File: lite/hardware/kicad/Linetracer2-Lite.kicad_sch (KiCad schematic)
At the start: 30 parts, among them J1 BATTERY (AA x3, XH 2P), J2 I2C (0.96in OLED order), M1 LEFT motor FA-130RA, M2 RIGHT motor FA-130RA, Q1 2SC1815-GR, SW1 START, U1 Raspberry Pi Pico, U2 AE-TC78H653FTG

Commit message: Lite rev.L2: XIAO ESP32C6 と LBR-127HLD に変更、子ども向けに配置・シルクを見直し
- マイコンを Seeed Studio XIAO ESP32C6（秋月 129481）に。ピンヘッダなしで基板にじかにはんだ付け
  （自作フットプリント: 裏のテストパッドの下は銅禁止、USB の足の逃げ穴、アンテナの下は両面銅なし）
- フォトリフレクタを LBR-127HLD（秋月 104500）に。背が 5.6 mm あるのでスキッドを 7.5 mm に
  （skid_clip_h70/h75/h80.stl、ロボットは後ろに 2.9° 傾く。傾きとすき間は scad で計算）
- いらない部品: I2C の穴 J2 を削除。電池電圧の測定はなし（XIAO の ADC 3 本をセンサーで使い切る）
- ピン割り当ては ESP32-C6 の起動時の状態に合わせ、どの瞬間もモーターが回らないようにした
- 基板を 65 x 100 mm の長方形に（面積 -27%、3D プリント部品はそのまま）、抵抗を 6 mm おきに
- シルクは記号だけ（つくる順番の数字、＋、LED の絵、抵抗の 3 本目の色）。説明は手順書 lite/docs/assembly.md
- gen_3d.py の 3D モデルの位置ずれを修正（KiCad は VRML の translation に scale をかけない）
- ERC 0、DRC 0（警告 0・未接続 0）。MicroPython (ESP32_GENERIC_C6) のライブラリとサンプルを移植

Co-Authored-By: Claude Opus 5.5 <noreply@anthropic.com>
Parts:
- removed J2: I2C (0.96in OLED order), Connector_PinHeader_2.54mm:PinHeader_1x04_P2.54mm_Vertical, symbol Connector_Generic:Conn_01x04
- C2: Note hold-up for Pico when motors pull the battery down -> hold-up for the XIAO when motors pull the battery down
- PS1, PS2, PS3: value LBR-123F -> LBR-127HLD; footprint Linetracer2:LBR-123F -> Linetracer2:LBR-127HLD; symbol Linetracer2:LBR-123F -> Linetracer2:LBR-127HLD; Akizuki 116455 -> 104500
- U1: value Raspberry Pi Pico -> XIAO ESP32C6; footprint Linetracer2:RaspberryPi_Pico_DirectSolder -> Linetracer2:XIAO_ESP32C6_DirectSolder; symbol Linetracer2:RaspberryPi_Pico_THT -> Linetracer2:XIAO_ESP32C6; Akizuki 116132 (Pico, Pico 2 also OK; not Pico W) -> 129481 (Seeed Studio XIAO ESP32C6)
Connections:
- net I2C_SCL is gone; now on net LED1: U1.7 (GPIO16/TX/D6)
- net I2C_SDA is gone; now on net MOT_IN2: U1.6 (GPIO23/SCL/D5)
- net +3V3: now also U1.12 (3V3); no longer U1.36 (3V3)
- net GND: no longer U1.18 (GND), U1.23 (GND), U1.28 (GND), U1.3 (GND), U1.33 (AGND), U1.38 (GND), U1.8 (GND)
- net LED1: no longer U1.24 (GPIO18)
- net MOT_IN1: now also U1.11 (GPIO18/MOSI/D10); no longer U1.16 (GPIO12)
- net MOT_IN2: no longer U1.17 (GPIO13)
- net MOT_IN3: now also U1.10 (GPIO20/MISO/D9); no longer U1.19 (GPIO14)
- net MOT_IN4: now also U1.9 (GPIO19/SCK/D8); no longer U1.20 (GPIO15)
- net MOT_OUT3: now also C4.2, M2.2 (-); no longer C4.1, M2.1 (+)
- net MOT_OUT4: now also C4.1, M2.1 (+); no longer C4.2, M2.2 (-)
- net MOT_STBY: now also U1.8 (GPIO17/RX/D7); no longer U1.15 (GPIO11)
- net SENS1: now also U1.3 (GPIO2/A2/D2); no longer U1.34 (GPIO28_ADC2)
- net SENS2: now also U1.2 (GPIO1/A1/D1); no longer U1.32 (GPIO27_ADC1)
- net SENS3: now also U1.1 (GPIO0/A0/D0); no longer U1.31 (GPIO26_ADC0)
- net SENS_LED_EN: now also U1.5 (GPIO22/SDA/D4); no longer U1.2 (GPIO1)
- net SW1: now also U1.4 (GPIO21/D3); no longer U1.21 (GPIO16)
- net VSYS: now also U1.14 (5V); no longer U1.39 (VSYS)
- no-connect marks 17 -> 0
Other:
- note added: "2. MCU Seeed Studio XIAO ESP32C6 (soldered flat, no pin headers)"
- note added: "5. LINE SENSORS 3 x LBR-127HLD (mount on the BOTTOM side, lens to the floor), 12 mm apart"
- note added: "Battery voltage is NOT measured: the XIAO has 3 ADC pins only (D0..D2) and the sensors use all of them."
- note added: "Bottom of the XIAO: bare test pads (BAT+, 3V3, BOOT, EN, JTAG) -> copper keep-out under them on the PCB."
- note added: "GPIO15 = yellow user LED on the XIAO (on = 0), a 2nd indicator for free. BOOT / RESET buttons are on the XIAO."
- note added: "GPIO16 (TX) / GPIO17 (RX) pull-up after reset + boot log / UART REPL -> no button and no motor input there."
- note added: "IN1/IN2 -> OUT1/OUT2 = LEFT motor, IN3/IN4 -> OUT3/OUT4 = RIGHT motor (+ = OUT4)"
- note added: "IR LED: (3.3V - 1.2V - 0.1V) / 100 ohm = about 20 mA each. Q1 switches all LEDs (ambient light cancel). Photo transistor: 10k pull-up -> white = low voltage, black = high voltage"
- note added: "Inside the XIAO: 5V pin -> Schottky -> buck regulator -> 3V3 (3V3 stays up while VBAT > about 4 V)."
- note added: "Linetracer2 Lite rev.L2 : XIAO ESP32C6 without pin headers, 3 x LBR-127HLD, 1 button, 1 LED"
- note added: "Never solder a Li-ion cell to the XIAO's BAT pads on this robot (AA cells are on the 5V pin)."
- note added: "PS1 = LEFT -> D2 (GPIO2/ADC), PS2 = CENTRE -> D1 (GPIO1/ADC), PS3 = RIGHT -> D0 (GPIO0/ADC) (seen from above, robot moving up the page)"
- note added: "Power: AA x3 (alkaline 4.5V recommended / NiMH 3.6V) -> VBAT (motors) ; VBAT -> D1 Schottky -> VSYS -> XIAO 5V pin. USB 5V can not back-feed the batteries. Never use 4 cells (the XIAO's 5V input clamps above about 6 V)."
- note added: "Q1: all IR LEDs on when SENS_LED_EN = 1 (about 60 mA)"
- note added: "Reset state (ESP32-C6 datasheet): GPIO18-23 weak pull-up during reset, then floating;"
- note added: "The body is 5.6 mm tall: the front of the robot is lifted by a 7.5 mm skid (lens about 2.3 mm above the floor)"
- note added: "XIAO 5V pin = USB VBUS: an external supply needs a diode (D1), otherwise USB 5V charges the AA cells."
- note added: "no buzzer, no power LED on the Lite board. 2nd indicator: the yellow user LED of the XIAO (GPIO15)"
- note removed: "2. MCU Raspberry Pi Pico / Pico 2 (soldered flat, no pin headers)"
- note removed: "5. EXPANSION (holes only)"
- note removed: "6. LINE SENSORS 3 x LBR-123F (mount on the BOTTOM side, lens to the floor, 2-3 mm gap), 12 mm apart"
- note removed: "Battery voltage: no divider on this board. The Pico measures VSYS/3 on GP29 (ADC3) internally;"
- note removed: "GP25 = on-board LED (a 2nd indicator for free). GP29/ADC3 = VSYS/3, GP24 = VBUS sense (inside Pico)."
- note removed: "IN1/IN2 -> OUT1/OUT2 = LEFT motor, IN3/IN4 -> OUT3/OUT4 = RIGHT motor"
- note removed: "IR LED: (3.3V - 1.25V) / 100 ohm = about 19 mA each. Q1 switches all LEDs (ambient light cancel). Photo transistor: 10k pull-up -> white = low voltage, black = high voltage"
- note removed: "Linetracer2 Lite : low-cost version (Pico without pin headers, 3 sensors, 1 button, 1 LED)"
- note removed: "PS1 = LEFT -> GP28/ADC2, PS2 = CENTRE -> GP27/ADC1, PS3 = RIGHT -> GP26/ADC0 (seen from above, robot moving up the page)"
- note removed: "Pico W / Pico 2 W: GP29 and GP25 belong to the radio chip -> battery reading does not work, not recommended."
- note removed: "Power: AA x3 (alkaline 4.5V / NiMH 3.6V) -> VBAT (motors) ; VBAT -> D1 Schottky -> VSYS (Pico). USB 5V can not back-feed the batteries. Never use 4 cells (Pico VSYS max 5.5V)."
- note removed: "Q1: all IR LEDs on when SENS_LED_EN = 1 (about 57 mA)"
- note removed: "VBAT = VSYS + about 0.3 V (D1). GP24 = 1 while USB is plugged in."
- note removed: "no buzzer, no power LED on the Lite board"
- title: Linetracer2 Lite - low-cost kids line tracer -> Linetracer2 Lite rev.L2 - XIAO ESP32C6 kids line tracer

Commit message: Lite rev.L3 基板: XIAO をピンヘッダで、ブザー追加、配線を手で引き直し、シルクを改良
- XIAO ESP32C6 を 2 列 x 7 ピンのスルーホール（ピンヘッダ）に。直付け用フットプリントは削除
- 圧電スピーカー BZ1（PKM13EPYH4000-A0）＋ R9 100 Ω を赤 LED と同じ D6 に
- 自動配線をやめ、lite/scripts/layout_lite.py に配置と配線を書いた（縦・横・45°、直角は面取り、
  バスで並べる、表で交差なし、ビア 0）。route_lite.py で KiCad に入れる。build_pcb.py は Lite では手配線
- 線が交差しないようにピンを 2 か所入れかえ（D3⇄D4、D8⇄D10）
- シルク: 抵抗の絵と ①ちゃ ②だいだい ③あか、つくる順番 ①〜⑮、電解コンデンサの黒い半分に白い −、
  センサーの ● / ○ / ◤
- 配置の確認用の絵: lite/scripts/preview_layout.py（KiCad なしで動く）
- DRC 0・未接続 0・回路図との不一致 0、ERC 0

Co-Authored-By: Claude Opus 5.5 <noreply@anthropic.com>
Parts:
- added BZ1: piezo 13mm, Linetracer2:Buzzer_PKM13_P5.0, symbol Device:Buzzer
- added R9: 100, Resistor_THT:R_Axial_DIN0207_L6.3mm_D2.5mm_P10.16mm_Horizontal, symbol Device:R
- U1: footprint Linetracer2:XIAO_ESP32C6_DirectSolder -> Linetracer2:XIAO_ESP32C6_Header; Akizuki 129481 (Seeed Studio XIAO ESP32C6) -> 129481 (Seeed Studio XIAO ESP32C6) + pin header 1x40 100167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; Note solder the castellated edge straight onto the pads, no pin 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 -> solder the XIAO on two 1x7 pin headers (cut from a 1x40 str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
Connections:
- net GND: now also BZ1.2 (-)
- net LED1: now also R9.1
- net MOT_IN1: now also U1.9 (GPIO19/SCK/D8); no longer U1.11 (GPIO18/MOSI/D10)
- net MOT_IN4: now also U1.11 (GPIO18/MOSI/D10); no longer U1.9 (GPIO19/SCK/D8)
- net SENS_LED_EN: now also U1.4 (GPIO21/D3); no longer U1.5 (GPIO22/SDA/D4)
- net SW1: now also U1.5 (GPIO22/SDA/D4); no longer U1.4 (GPIO21/D3)
- new net: BZ1.1 (+), R9.2
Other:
- note added: "2. MCU Seeed Studio XIAO ESP32C6 (on two 1x7 pin headers)"
- note added: "4. BUTTON / LED / BUZZER"
- note added: "Linetracer2 Lite rev.L3 : XIAO ESP32C6 on pin headers, 3 x LBR-127HLD, 1 button, 1 LED, 1 buzzer"
- note added: "On pin headers the XIAO sits 2.5 mm above the board: its bare bottom test pads can not touch the tracks."
- note added: "The buzzer shares D6 (LED1) with the red LED (no free XIAO pin): LED on = DC -> the piezo is silent;"
- note added: "beep = PWM (1-4 kHz) -> the LED glows while it beeps. No power LED. 2nd LED: the XIAO's yellow LED (GPIO15)"
- note removed: "2. MCU Seeed Studio XIAO ESP32C6 (soldered flat, no pin headers)"
- note removed: "4. BUTTON / LED"
- note removed: "Bottom of the XIAO: bare test pads (BAT+, 3V3, BOOT, EN, JTAG) -> copper keep-out under them on the PCB."
- note removed: "Linetracer2 Lite rev.L2 : XIAO ESP32C6 without pin headers, 3 x LBR-127HLD, 1 button, 1 LED"
- note removed: "no buzzer, no power LED on the Lite board. 2nd indicator: the yellow user LED of the XIAO (GPIO15)"
- title: Linetracer2 Lite rev.L2 - XIAO ESP32C6 kids line tracer -> Linetracer2 Lite rev.L3 - XIAO ESP32C6 kids line tracer

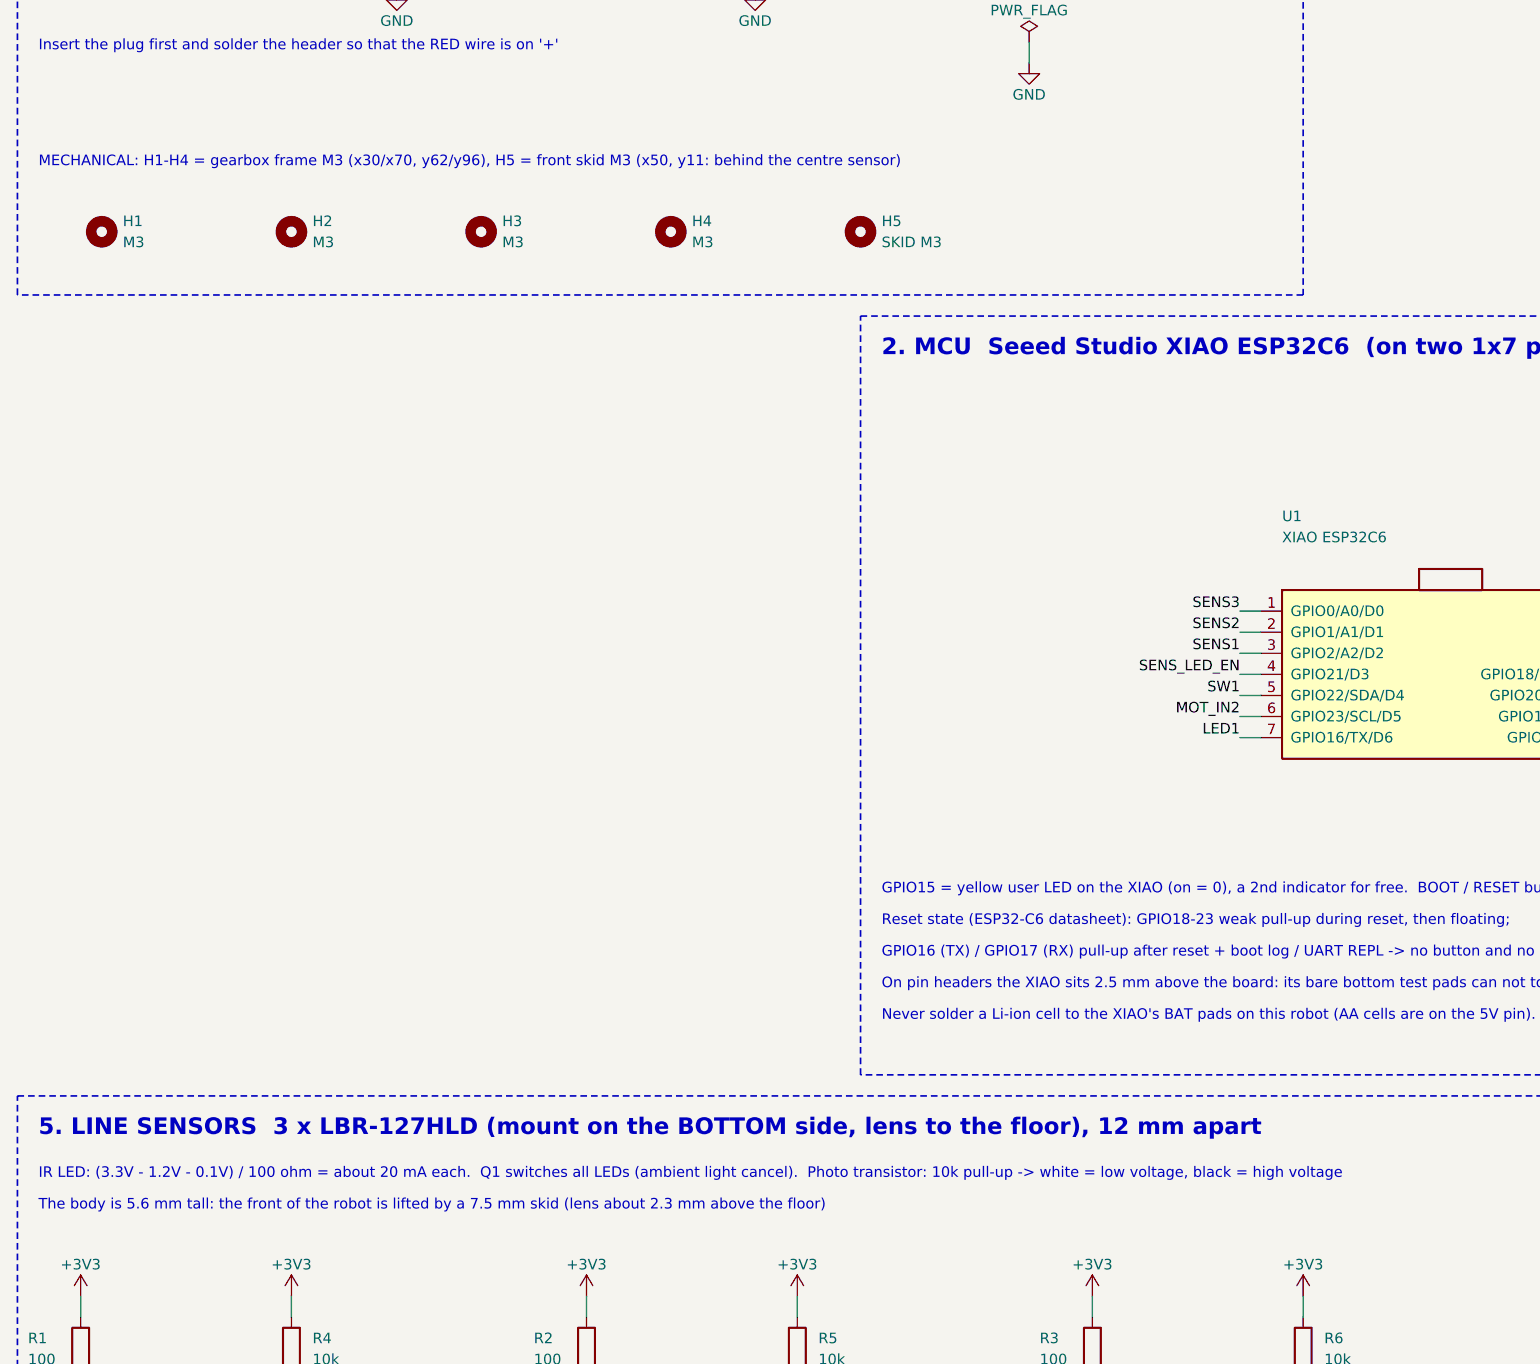
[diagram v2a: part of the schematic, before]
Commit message: 子ども向けレビューの反映: 向きの印・手順・安全・ソフト、手順ごとの絵
- シルク: モータードライバーに「VM」、電解コンデンサの丸の外にも − / ＋（付けたあとも確かめられる）、
  KiCad の小さい ＋ を消した、LED の − を四角い穴に、⑭ うら、2 けたの番号を大きく
- つくる順番: ⑪ モータードライバー → ⑫ XIAO → ⑬ 470 µF（いちばん背が高いので最後）
- J1 のパッドを 1.5 mm 幅に（＋ と − の間 0.7 → 1.0 mm）
- 手順書: こども用（ひらがな）と先生用の列、手順ごとの絵（lite/scripts/step_images.py）、電気を入れる前の
  先生チェック（向き・テスター・D1）、電池は最後まで入れない、保護めがね、うごかしかたカード
- ソフト: キャリブレーションの前に 1 秒待つ、判定 CAL_MIN_SPAN 4000、長押し 1.5 秒＋カチッ、
  音量 robot.volume としずかモード、Ctrl-C でもモーターを止める（motors.off）

Co-Authored-By: Claude Opus 5.5 <noreply@anthropic.com>
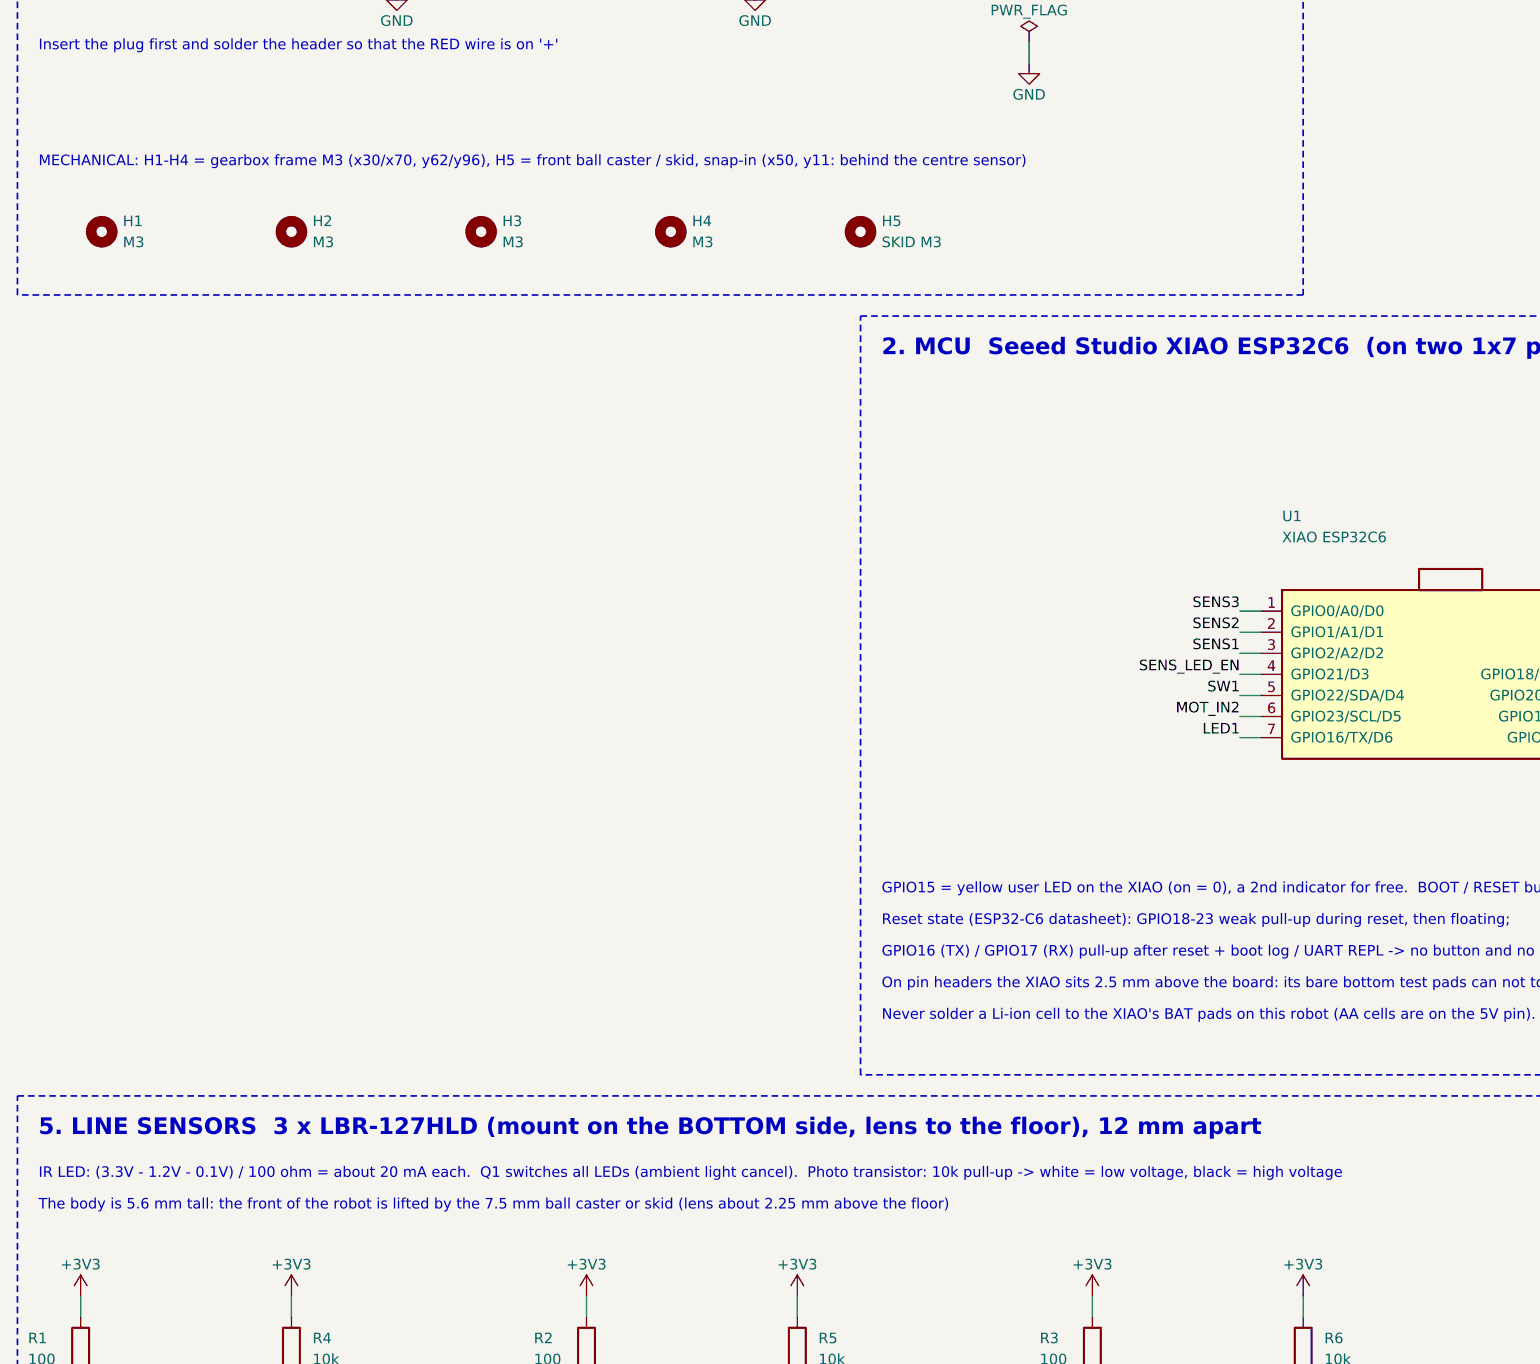
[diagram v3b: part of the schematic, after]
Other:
- note added: "MECHANICAL: H1-H4 = gearbox frame M3 (x30/x70, y62/y96), H5 = front ball caster / skid, snap-in (x50, y11: behind the centre sensor)"
- note added: "The body is 5.6 mm tall: the front of the robot is lifted by the 7.5 mm ball caster or skid (lens about 2.25 mm above the floor)"
- note removed: "MECHANICAL: H1-H4 = gearbox frame M3 (x30/x70, y62/y96), H5 = front skid M3 (x50, y11: behind the centre sensor)"
- note removed: "The body is 5.6 mm tall: the front of the robot is lifted by a 7.5 mm skid (lens about 2.3 mm above the floor)"
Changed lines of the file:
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@@
 		)
 	)
-	(text "MECHANICAL: H1-H4 = gearbox frame M3 (x30/x70, y62/y96), H5 = front skid M3 (x50, y11: behind the centre sensor)"
+	(text "MECHANICAL: H1-H4 = gearbox frame M3 (x30/x70, y62/y96), H5 = front ball caster / skid, snap-in (x50, y11: behind the centre sensor)"
 		(exclude_from_sim no)
 		(at 20.32 83.82 0)
@@
 		)
 	)
-	(text "The body is 5.6 mm tall: the front of the robot is lifted by a 7.5 mm skid (lens about 2.3 mm above the floor)"
+	(text "The body is 5.6 mm tall: the front of the robot is lifted by the 7.5 mm ball caster or skid (lens about 2.25 mm above the floor)"
 		(exclude_from_sim no)
 		(at 20.32 209.55 0)
